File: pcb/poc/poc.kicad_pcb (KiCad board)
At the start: 2 copper layers, 100 x 100 mm, 62 parts, among them J1 USB_B_Mini, J2 Right, J3 Left, J4 AVR-ISP-6, J5 Conn_02x10_Odd_Even, J6 Conn_02x08_Odd_Even, J7 Conn_01x02, J8 Conn_01x02, SW1 SW_Push, SW10 SW_Push_45deg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

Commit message: pcb: poc: Change track to 0.4mm
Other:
- net class Default: trace_width 0.25 -> 0.4

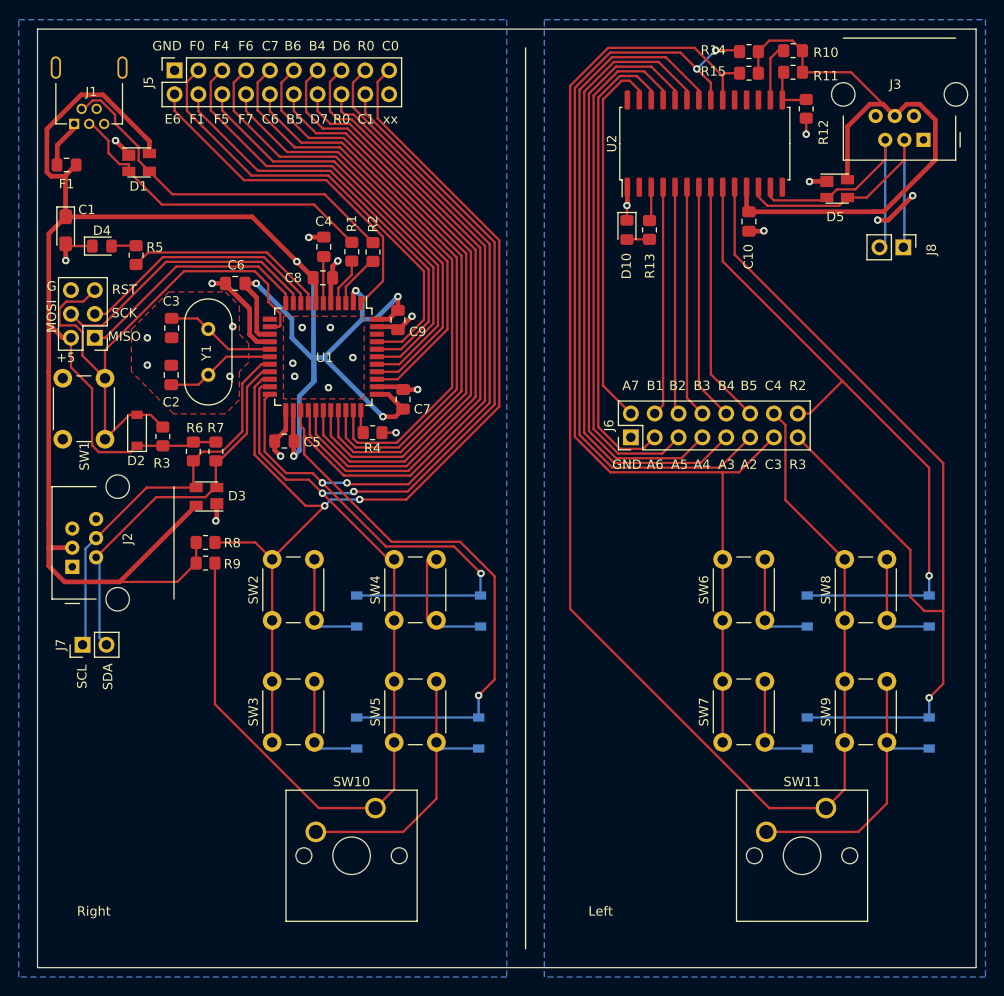
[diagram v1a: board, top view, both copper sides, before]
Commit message: pcb: poc: Space out left side
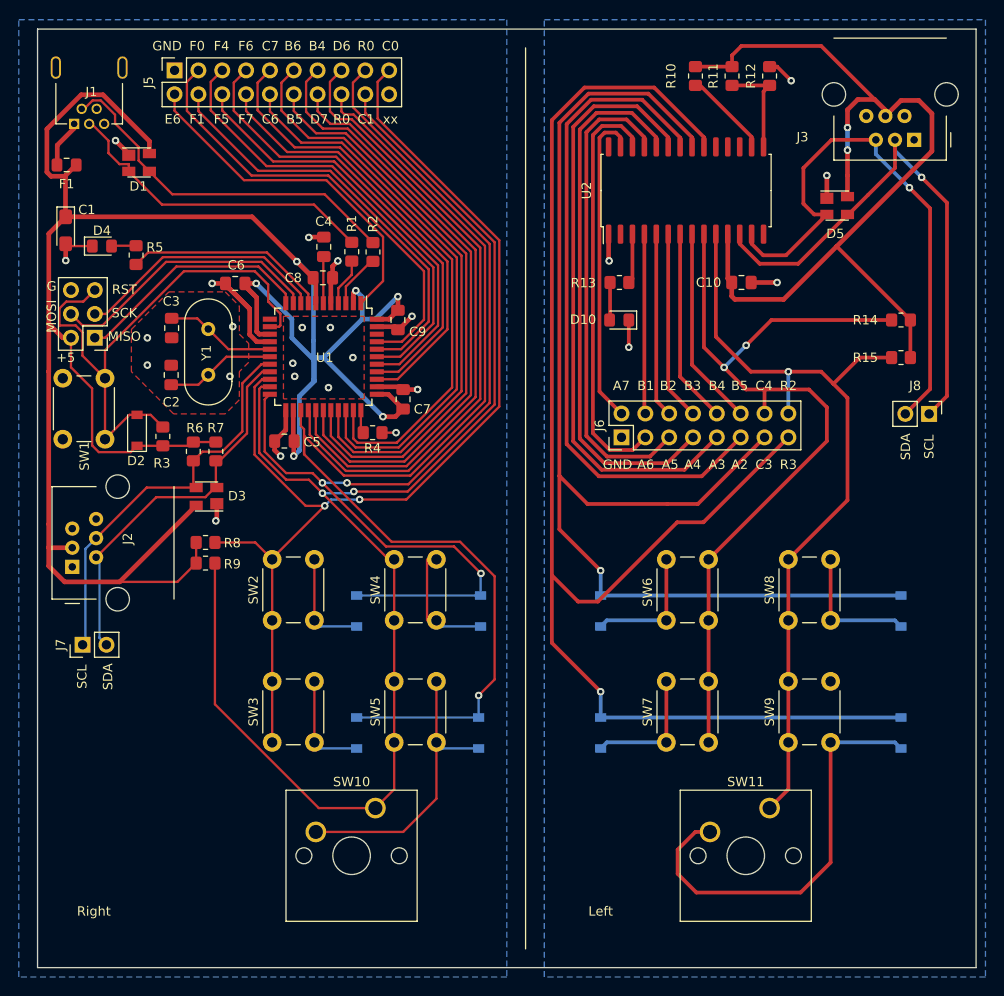
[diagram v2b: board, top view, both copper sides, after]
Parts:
- moved R15 34.4 mm to (162.0, 90.0)
- moved R14 32.9 mm to (162.0, 86.0)
- moved D11 22.0 mm to (130.0, 117.0)
- moved D12 22.0 mm to (130.0, 130.0)
- moved J8 18.0 mm to (165.0, 96.0)
- moved R10 10.7 mm to (140.1, 60.0), turned to 270 degrees
- moved D10 9.64 mm to (132.0, 86.0), turned to 180 degrees
- moved SW6 6.67 mm to (141.5, 111.5), turned to 270 degrees
- moved SW7 6.67 mm to (141.5, 124.5), turned to 270 degrees
- moved C10 6.55 mm to (145.0, 82.0), turned to 0 degrees
- moved R11 6.51 mm to (144.0, 60.0), turned to 90 degrees
- moved R13 6.45 mm to (132.0, 82.0), turned to 180 degrees
- moved SW11 6.00 mm to (148.0, 138.0)
- moved SW8 6.00 mm to (150.0, 118.0)
- moved SW9 6.00 mm to (150.0, 131.0)
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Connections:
- J6 pad 13: /COL3 -> /ROW2
- J6 pad 14: /COL4 -> /COL3
- J6 pad 16: /ROW2 -> /COL4
- U2 pad 10: /ROW3 -> /COL4
- U2 pad 20: /COL4 -> /ROW3
- U2 pad 21: /COL3 -> /ROW2
- U2 pad 9: /ROW2 -> /COL3
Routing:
- net /COL4: track 161.4 -> 86.6 mm, vias 0 -> 1
- net /ROW2: track 71.8 -> 128.6 mm
- net /ROW3: track 105.4 -> 152.3 mm
- net /SDA1: track 29.0 -> 59.8 mm, vias 0 -> 1
- net +5VP: track 68.9 -> 98.0 mm, vias 0 -> 2
- net /SCL1: track 32.6 -> 58.0 mm, vias 0 -> 1
- net /COL3: track 114.9 -> 91.2 mm
- net Net-(D14-Pad2): track 31.9 -> 45.8 mm
- net /GPA7: track 40.8 -> 34.1 mm
- net /GPA6: track 50.8 -> 44.8 mm
- net /GPB1: track 24.5 -> 19.2 mm
- net Net-(R11-Pad1): track 5.58 -> 10.8 mm
- net /GPA5: track 56.7 -> 51.5 mm
- net /GPB5: track 25.8 -> 21.3 mm
- net /GPB4: track 25.3 -> 20.7 mm
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
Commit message: pcb: poc: routed left side except breakout
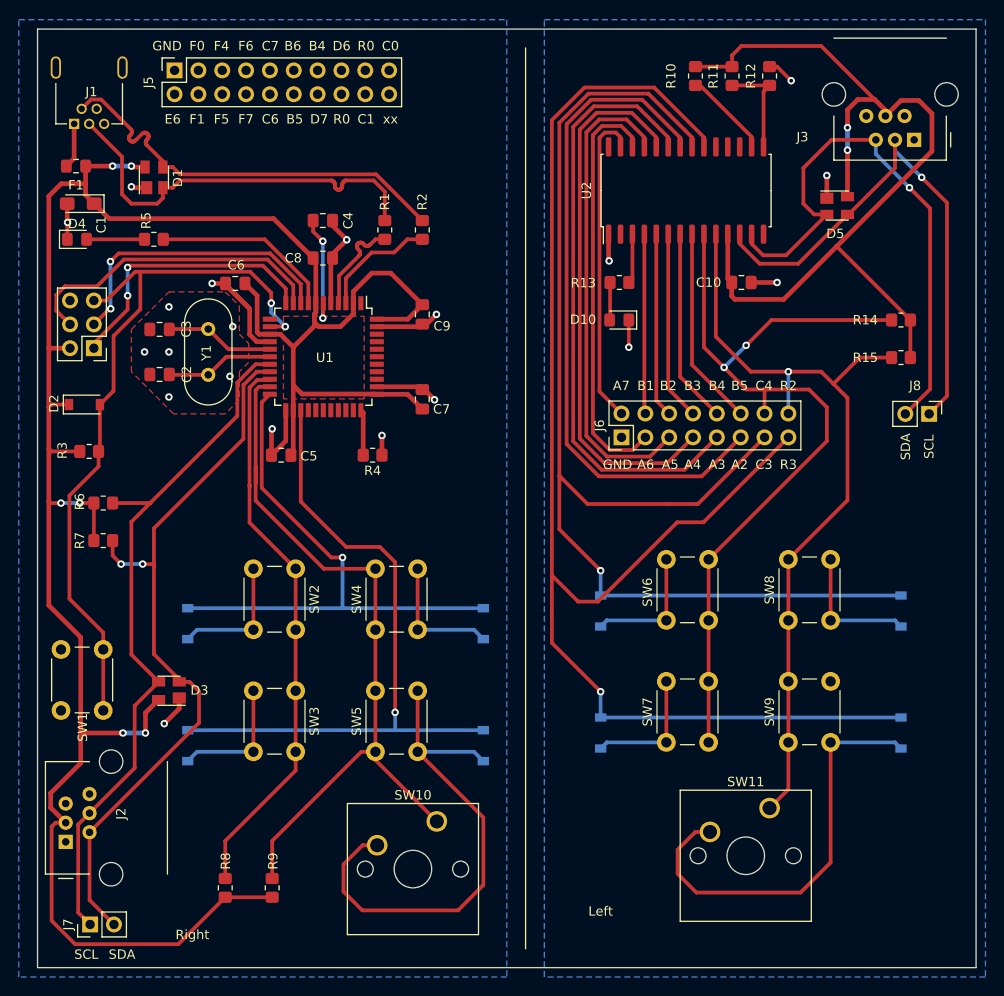
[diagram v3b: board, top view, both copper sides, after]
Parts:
- moved R8 36.9 mm to (90.0, 146.5), turned to 90 degrees
- moved R9 35.3 mm to (95.0, 146.5), turned to 90 degrees
- moved J7 29.8 mm to (75.6, 150.4)
- moved J2 29.3 mm to (73.0, 141.6)
- moved SW1 28.9 mm to (72.5, 127.6)
- moved D3 21.1 mm to (84.0, 125.5)
- moved D6 18.1 mm to (86.0, 118.3)
- moved D7 18.1 mm to (86.0, 131.3)
- moved R7 15.3 mm to (77.0, 109.5), turned to 0 degrees
- moved R6 11.1 mm to (77.0, 105.5), turned to 0 degrees
- moved R3 8.01 mm to (75.5, 100.0), turned to 0 degrees
- moved SW10 6.69 mm to (112.5, 139.4)
- moved D2 6.24 mm to (75.0, 95.0), turned to 0 degrees
- moved SW2 6.04 mm to (97.5, 112.5), turned to 270 degrees
- moved SW3 6.04 mm to (97.5, 125.5), turned to 270 degrees
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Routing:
- net /COL1: track 152.2 -> 80.2 mm, vias 2 -> 0
- net /PD6: track 68.6 -> 0.00 mm
- net /PB4: track 66.4 -> 0.00 mm
- net /PD7: track 64.5 -> 0.00 mm
- net /PB6: track 64.2 -> 0.00 mm
- net /PB5: track 62.2 -> 0.00 mm
- net /PC7: track 61.9 -> 0.00 mm
- net /PC6: track 60.0 -> 0.00 mm
- net /COL0: track 118.0 -> 60.2 mm, vias 2 -> 0
- net /ROW0: track 113.9 -> 58.9 mm, vias 3 -> 1
- net /ROW1: track 125.2 -> 71.9 mm
- net /PF6: track 49.7 -> 0.00 mm
- net /PF4: track 48.9 -> 0.00 mm
- net /PF0: track 48.3 -> 0.00 mm
- net /PF7: track 46.8 -> 0.00 mm
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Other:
- board text removed: "+5"
- board text removed: "G"
- board text removed: "MISO"
- board text removed: "MOSI"
- board text removed: "RST"
- board text removed: "SCK"

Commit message: pcb: poc: Route left breakout
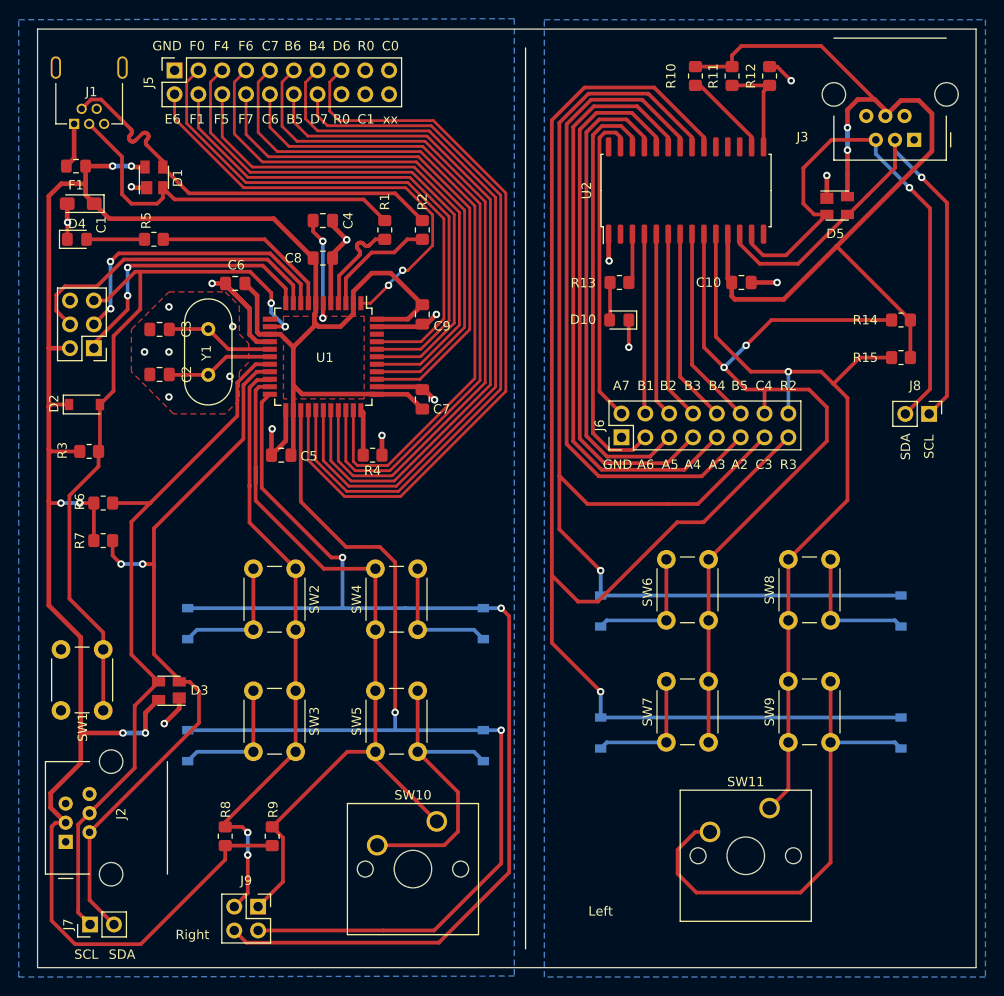
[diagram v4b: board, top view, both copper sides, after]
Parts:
- added J9: Conn_02x02_Odd_Even, Connector_PinSocket_2.54mm:PinSocket_2x02_P2.54mm_Vertical, F.Cu at (93.5, 148.5)
- moved R8 5.50 mm to (90.0, 141.0)
- moved R9 5.50 mm to (95.0, 141.0)
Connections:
- J5 pad 16: /ROW1 -> Net-(J5-Pad16)
- J5 pad 17: /ROW0 -> Net-(J5-Pad17)
- J5 pad 18: /COL1 -> Net-(J5-Pad18)
- J5 pad 19: /COL0 -> Net-(J5-Pad19)
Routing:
- net /PD6: track 0.00 -> 81.0 mm
- net /PB4: track 0.00 -> 78.8 mm
- net /PD7: track 0.00 -> 76.9 mm
- net /PB6: track 0.00 -> 76.6 mm
- net /PB5: track 0.00 -> 74.6 mm
- net /PC7: track 0.00 -> 74.3 mm
- net /PC6: track 0.00 -> 72.3 mm
- net /ROW0: track 58.9 -> 122.3 mm, vias 1 -> 2
- net /PF6: track 0.00 -> 59.0 mm
- net /PF4: track 0.00 -> 58.0 mm
- net /PF0: track 0.00 -> 56.6 mm
- net /PF7: track 0.00 -> 56.4 mm
- net /PF5: track 0.00 -> 55.7 mm
- net /PF1: track 0.00 -> 54.3 mm
- net /PE6: track 0.00 -> 47.9 mm, vias 0 -> 2
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
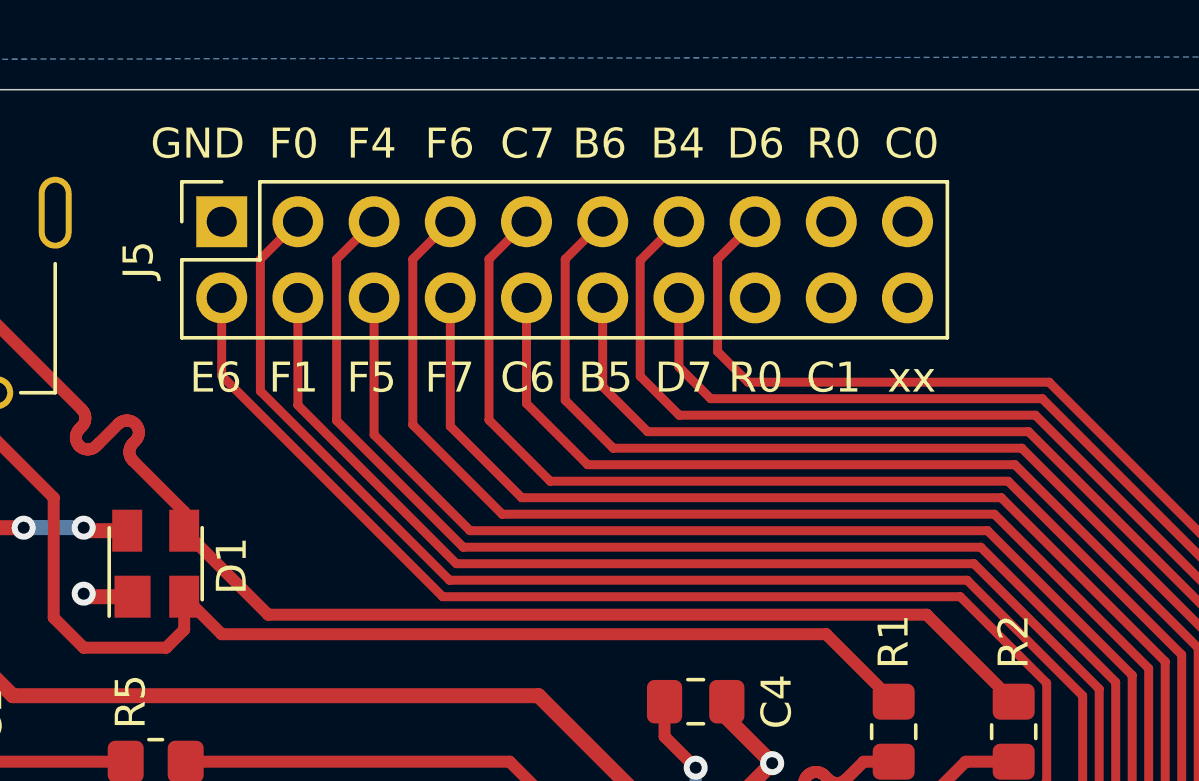
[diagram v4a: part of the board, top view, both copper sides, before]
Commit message: pcb: poc: Make left breakout smaller
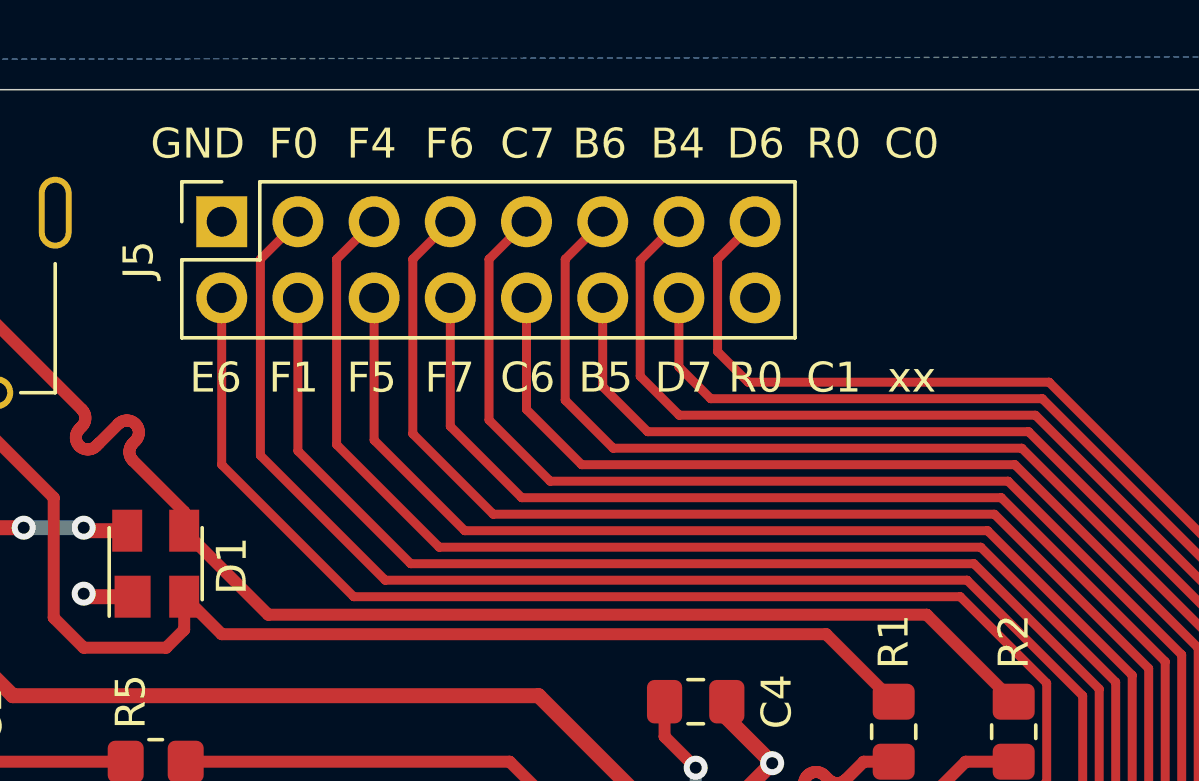
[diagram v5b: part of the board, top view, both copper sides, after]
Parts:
- J5: value Conn_02x10_Odd_Even -> Conn_02x08_Odd_Even; footprint Connector_PinSocket_2.54mm:PinSocket_2x10_P2.54mm_Vertical -> Connector_PinSocket_2.54mm:PinSocket_2x08_P2.54mm_Vertical
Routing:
- net /PE6: track 47.9 -> 49.6 mm
- net /PF0: track 56.6 -> 57.9 mm
- net /PF1: track 54.3 -> 55.2 mm
